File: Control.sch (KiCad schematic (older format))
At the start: 21 parts

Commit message: version preliminar de la etapa de alimentacion
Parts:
- gave numbers to parts that had none: 21
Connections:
- wire segments 81 -> 71

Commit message: asignacion inicial de huellas
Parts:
- added C37: 10n, Capacitors_SMD:C_0805, symbol C
- added C38, C39: 0,047n, Capacitors_SMD:C_0805, symbol C
- added D3: D_Schottky_ALT, Diodos:SOD-123, symbol D_Schottky_ALT
- added F2: F, Resistencias:R_1812, symbol F
- added L3: Ferrita, Capacitors_SMD:C_0805, symbol Ferrita
- added P15: USB_MINI, Conectores:usb_mini_molex_675031020, symbol USB_MINI
- added R60, R61: 22R, Resistencias:R_0805, symbol R
- C10, C5, C6, C8, C9: footprint (none) -> Capacitors_SMD:C_0805
- C11: footprint (none) -> Capacitors_SMD:C_1210
- C7: footprint (none) -> Capacitors_SMD:C_1206
- R10, R11, R3, R4, R5, R6, R7, R8, R9: footprint (none) -> Resistencias:R_0805
- U3: footprint (none) -> Housings_SSOP:SSOP-20_4.4x6.5mm_Pitch0.65mm
- U4: footprint (none) -> esp:ESP-12E
- Y1: footprint (none) -> Cristal:Cristal_SMD_HC49-SD; Fabricante (none) -> Fox Electronics; Provedor (none) -> rs; Ref (none) -> FOXSDLF/120-20; Ref_Proveedor (none) -> 547-6480
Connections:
- net labels added: VUSB
- wire segments 71 -> 90
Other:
- moved on the sheet: C10, C11, R3, R4, R5, R6, R7, U4

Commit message: cambiar ch340T por ch340g y añadir nc a pines
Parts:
- removed U3: CH340T, Housings_SSOP:SSOP-20_4.4x6.5mm_Pitch0.65mm, symbol CH340T
- added U3: CH340G, Housings_SOIC:SOIC-16_3.9x9.9mm_Pitch1.27mm, symbol CH340G
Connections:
- no-connect marks 7 -> 15
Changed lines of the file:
@@
 $Descr A4 11693 8268
 encoding utf-8
-Sheet 3 15
+Sheet 3 14
 Title ""
 Date "2017-01-15"
@@
 Comment4 "Wifi Play Board"
 $EndDescr
-$Comp
-L CH340T U3
-U 1 1 583CB227
-P 2550 3650
-F 0 "U3" H 2600 3600 60  0000 C CNN
-F 1 "CH340T" H 3000 4000 80  0000 C CNN
-F 2 "Housings_SSOP:SSOP-20_4.4x6.5mm_Pitch0.65mm" H 2750 3650 60  0001 C CNN
-F 3 "" H 2750 3650 60  0001 C CNN
-F 4 "~" H 2550 3650 60  0001 C CNN "Fabricante"
-F 5 "~" H 2550 3650 60  0001 C CNN "Ref"
-F 6 "~" H 2550 3650 60  0001 C CNN "Potencia"
-F 7 "~" H 2550 3650 60  0001 C CNN "Tolerancia"
-F 8 "~" H 2550 3650 60  0001 C CNN "Provedor"
-F 9 "~" H 2550 3650 60  0001 C CNN "Ref_Proveedor"
-	1    2550 3650
-	1    0    0    -1
-$EndComp
 $Comp
 L ESP8266 U4
@@
 Connection ~ 1350 3450
 $Comp
-L GND #PWR016
+L GND #PWR024
 U 1 1 583CD0A6
 P 1350 4050
-F 0 "#PWR016" H 1350 3800 50  0001 C CNN
+F 0 "#PWR024" H 1350 3800 50  0001 C CNN
 F 1 "GND" H 1355 3877 50  0000 C CNN
 F 2 "" H 1350 4050 50  0000 C CNN
@@
 $EndComp
 $Comp
-L GND #PWR017
+L GND #PWR025
 U 1 1 583CD111
 P 1950 4050
-F 0 "#PWR017" H 1950 3800 50  0001 C CNN
+F 0 "#PWR025" H 1950 3800 50  0001 C CNN
 F 1 "GND" H 1955 3877 50  0000 C CNN
 F 2 "" H 1950 4050 50  0000 C CNN
@@
 $EndComp
 $Comp
-L GND #PWR018
+L GND #PWR026
 U 1 1 583E093D
 P 9550 5300
-F 0 "#PWR018" H 9550 5050 50  0001 C CNN
+F 0 "#PWR026" H 9550 5050 50  0001 C CNN
 F 1 "GND" H 9555 5127 50  0000 C CNN
 F 2 "" H 9550 5300 50  0000 C CNN
@@
 	9550 5100 9450 5100
 $Comp
-L GND #PWR019
+L GND #PWR027
 U 1 1 583E0A57
 P 7400 5850
-F 0 "#PWR019" H 7400 5600 50  0001 C CNN
+F 0 "#PWR027" H 7400 5600 50  0001 C CNN
 F 1 "GND" H 7405 5677 50  0000 C CNN
 F 2 "" H 7400 5850 50  0000 C CNN
@@
 	7250 5100 7550 5100
 $Comp
-L +3V3 #PWR020
+L +3V3 #PWR028
 U 1 1 583F255D
 P 7250 5100
-F 0 "#PWR020" H 7250 4950 50  0001 C CNN
+F 0 "#PWR028" H 7250 4950 50  0001 C CNN
 F 1 "+3V3" V 7265 5228 50  0000 L CNN
 F 2 "" H 7250 5100 50  0000 C CNN
@@
 Connection ~ 7400 5100
 $Comp
-L +5V #PWR021
+L +5V #PWR029
 U 1 1 583F2750
 P 2900 1150
-F 0 "#PWR021" H 2900 1000 50  0001 C CNN
+F 0 "#PWR029" H 2900 1000 50  0001 C CNN
 F 1 "+5V" H 2915 1323 50  0000 C CNN
 F 2 "" H 2900 1150 50  0000 C CNN
@@
 Connection ~ 2900 1300
 $Comp
-L GND #PWR022
+L GND #PWR030
 U 1 1 583F287E
 P 2150 1800
-F 0 "#PWR022" H 2150 1550 50  0001 C CNN
+F 0 "#PWR030" H 2150 1550 50  0001 C CNN
 F 1 "GND" H 2155 1627 50  0000 C CNN
 F 2 "" H 2150 1800 50  0000 C CNN
@@
 	2550 1700 2550 1800
 $Comp
-L GND #PWR023
+L GND #PWR031
 U 1 1 583F2984
 P 2550 1800
-F 0 "#PWR023" H 2550 1550 50  0001 C CNN
+F 0 "#PWR031" H 2550 1550 50  0001 C CNN
 F 1 "GND" H 2555 1627 50  0000 C CNN
 F 2 "" H 2550 1800 50  0000 C CNN
@@
 $EndComp
 $Comp
-L GND #PWR024
+L GND #PWR032
 U 1 1 583F2B88
 P 3050 4000
-F 0 "#PWR024" H 3050 3750 50  0001 C CNN
+F 0 "#PWR032" H 3050 3750 50  0001 C CNN
 F 1 "GND" H 3055 3827 50  0000 C CNN
 F 2 "" H 3050 4000 50  0000 C CNN
@@
 $EndBitmap
 $Comp
-L +3V3 #PWR025
+L +3V3 #PWR033
 U 1 1 583F38C9
 P 7750 1100
-F 0 "#PWR025" H 7750 950 50  0001 C CNN
+F 0 "#PWR033" H 7750 950 50  0001 C CNN
 F 1 "+3V3" H 7765 1273 50  0000 C CNN
 F 2 "" H 7750 1100 50  0000 C CNN
@@
 	7750 2050 7750 2450
 $Comp
-L GND #PWR026
+L GND #PWR034
 U 1 1 583F42FE
 P 7750 2450
-F 0 "#PWR026" H 7750 2200 50  0001 C CNN
+F 0 "#PWR034" H 7750 2200 50  0001 C CNN
 F 1 "GND" H 7755 2277 50  0000 C CNN
 F 2 "" H 7750 2450 50  0000 C CNN
@@
 NoConn ~ 3750 2850
 NoConn ~ 2350 2850
-NoConn ~ 2350 2700
 Text Label 8700 1450 2    60   ~ 0
 GPIO2
@@
 Wire Wire Line
 	4150 2250 3750 2250
-NoConn ~ 3750 3450
-$Comp
-L GND #PWR027
+$Comp
+L GND #PWR035
 U 1 1 587ABB0C
 P 3550 1800
-F 0 "#PWR027" H 3550 1550 50  0001 C CNN
+F 0 "#PWR035" H 3550 1550 50  0001 C CNN
 F 1 "GND" H 3555 1627 50  0000 C CNN
 F 2 "" H 3550 1800 50  0000 C CNN
@@
 MOSI
 $Comp
-L GND #PWR028
+L GND #PWR036
 U 1 1 587BEF34
 P 9100 2450
-F 0 "#PWR028" H 9100 2200 50  0001 C CNN
+F 0 "#PWR036" H 9100 2200 50  0001 C CNN
 F 1 "GND" H 9105 2277 50  0000 C CNN
 F 2 "" H 9100 2450 50  0000 C CNN
@@
 	3200 7000 3200 6650
 $Comp
-L GND #PWR029
+L GND #PWR037
 U 1 1 5891BD78
 P 2150 7000
-F 0 "#PWR029" H 2150 6750 50  0001 C CNN
+F 0 "#PWR037" H 2150 6750 50  0001 C CNN
 F 1 "GND" H 2155 6827 50  0000 C CNN
 F 2 "" H 2150 7000 50  0000 C CNN
@@
 $EndComp
 $Comp
-L GND #PWR030
+L GND #PWR038
 U 1 1 5891BD7E
 P 2700 7000
-F 0 "#PWR030" H 2700 6750 50  0001 C CNN
+F 0 "#PWR038" H 2700 6750 50  0001 C CNN
 F 1 "GND" H 2705 6827 50  0000 C CNN
 F 2 "" H 2700 7000 50  0000 C CNN
@@
 $EndComp
 $Comp
-L GND #PWR031
+L GND #PWR039
 U 1 1 5891BD84
 P 3200 7000
-F 0 "#PWR031" H 3200 6750 50  0001 C CNN
+F 0 "#PWR039" H 3200 6750 50  0001 C CNN
 F 1 "GND" H 3205 6827 50  0000 C CNN
 F 2 "" H 3200 7000 50  0000 C CNN
@@
 	4800 5800 4800 5600
 $Comp
-L +5V #PWR032
+L +5V #PWR040
 U 1 1 5891BD93
 P 4800 5600
-F 0 "#PWR032" H 4800 5450 50  0001 C CNN
+F 0 "#PWR040" H 4800 5450 50  0001 C CNN
 F 1 "+5V" H 4815 5773 50  0000 C CNN
 F 2 "" H 4800 5600 50  0000 C CNN
@@
 	3600 5250 3600 5800
 Connection ~ 3600 5800
+$Comp
+L CH340G U3
+U 1 1 58965F58
+P 2550 3650
+F 0 "U3" H 2600 3550 60  0000 C CNN
+F 1 "CH340G" H 3050 4000 80  0000 C CNN
+F 2 "Housings_SOIC:SOIC-16_3.9x9.9mm_Pitch1.27mm" H -350 750 60  0001 C CNN
+F 3 "" H -350 750 60  0001 C CNN
+	1    2550 3650
+	1    0    0    -1
+$EndComp
+NoConn ~ 8200 5500
+NoConn ~ 8300 5500
+NoConn ~ 8400 5500
+NoConn ~ 8500 5500
+NoConn ~ 8600 5500
+NoConn ~ 8700 5500
+NoConn ~ 7250 4700
+NoConn ~ 7250 4500
+NoConn ~ 2050 6100
+NoConn ~ 1650 6400
 $EndSCHEMATC

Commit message: cambiado cristal de cuarzo por resonador
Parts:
- removed C5, C6: 0,022n, Capacitors_SMD:C_0805, symbol C
- removed L3: Ferrita, Capacitors_SMD:C_0805, symbol Ferrita
- removed Y1: 12MHz, Cristal:Cristal_SMD_HC49-SD, symbol Cristal_2P
- added Y1: Cristal, Cristal:Murata_CSTCE_V_A, symbol Cristal
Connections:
- wire segments 90 -> 88
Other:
- moved on the sheet: C7, D3, F2

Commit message: place inicial sobre la pcb
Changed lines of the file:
@@
 USBD-
 $Comp
-L GND #PWR026
+L GND #PWR024
 U 1 1 583CD0A6
 P 1350 3400
-F 0 "#PWR026" H 1350 3150 50  0001 C CNN
+F 0 "#PWR024" H 1350 3150 50  0001 C CNN
 F 1 "GND" H 1355 3227 50  0000 C CNN
 F 2 "" H 1350 3400 50  0000 C CNN
@@
 $EndComp
 $Comp
-L GND #PWR028
+L GND #PWR025
 U 1 1 583E093D
 P 9550 5300
-F 0 "#PWR028" H 9550 5050 50  0001 C CNN
+F 0 "#PWR025" H 9550 5050 50  0001 C CNN
 F 1 "GND" H 9555 5127 50  0000 C CNN
 F 2 "" H 9550 5300 50  0000 C CNN
@@
 	9550 5100 9450 5100
 $Comp
-L GND #PWR029
+L GND #PWR026
 U 1 1 583E0A57
 P 7400 5850
-F 0 "#PWR029" H 7400 5600 50  0001 C CNN
+F 0 "#PWR026" H 7400 5600 50  0001 C CNN
 F 1 "GND" H 7405 5677 50  0000 C CNN
 F 2 "" H 7400 5850 50  0000 C CNN
@@
 	7250 5100 7550 5100
 $Comp
-L +3V3 #PWR030
+L +3V3 #PWR027
 U 1 1 583F255D
 P 7250 5100
-F 0 "#PWR030" H 7250 4950 50  0001 C CNN
+F 0 "#PWR027" H 7250 4950 50  0001 C CNN
 F 1 "+3V3" V 7265 5228 50  0000 L CNN
 F 2 "" H 7250 5100 50  0000 C CNN
@@
 Connection ~ 7400 5100
 $Comp
-L +5V #PWR031
+L +5V #PWR028
 U 1 1 583F2750
 P 2550 1150
-F 0 "#PWR031" H 2550 1000 50  0001 C CNN
+F 0 "#PWR028" H 2550 1000 50  0001 C CNN
 F 1 "+5V" H 2565 1323 50  0000 C CNN
 F 2 "" H 2550 1150 50  0000 C CNN
@@
 $EndComp
 $Comp
-L GND #PWR032
+L GND #PWR029
 U 1 1 583F287E
 P 4500 6550
-F 0 "#PWR032" H 4500 6300 50  0001 C CNN
+F 0 "#PWR029" H 4500 6300 50  0001 C CNN
 F 1 "GND" H 4505 6377 50  0000 C CNN
 F 2 "" H 4500 6550 50  0000 C CNN
@@
 	2550 1700 2550 1800
 $Comp
-L GND #PWR033
+L GND #PWR030
 U 1 1 583F2984
 P 2550 1800
-F 0 "#PWR033" H 2550 1550 50  0001 C CNN
+F 0 "#PWR030" H 2550 1550 50  0001 C CNN
 F 1 "GND" H 2555 1627 50  0000 C CNN
 F 2 "" H 2550 1800 50  0000 C CNN
@@
 $EndComp
 $Comp
-L GND #PWR034
+L GND #PWR031
 U 1 1 583F2B88
 P 3050 4000
-F 0 "#PWR034" H 3050 3750 50  0001 C CNN
+F 0 "#PWR031" H 3050 3750 50  0001 C CNN
 F 1 "GND" H 3055 3827 50  0000 C CNN
 F 2 "" H 3050 4000 50  0000 C CNN
@@
 $EndBitmap
 $Comp
-L +3V3 #PWR035
+L +3V3 #PWR032
 U 1 1 583F38C9
 P 7750 1100
-F 0 "#PWR035" H 7750 950 50  0001 C CNN
+F 0 "#PWR032" H 7750 950 50  0001 C CNN
 F 1 "+3V3" H 7765 1273 50  0000 C CNN
 F 2 "" H 7750 1100 50  0000 C CNN
@@
 	7750 2050 7750 2450
 $Comp
-L GND #PWR036
+L GND #PWR033
 U 1 1 583F42FE
 P 7750 2450
-F 0 "#PWR036" H 7750 2200 50  0001 C CNN
+F 0 "#PWR033" H 7750 2200 50  0001 C CNN
 F 1 "GND" H 7755 2277 50  0000 C CNN
 F 2 "" H 7750 2450 50  0000 C CNN
@@
 	4150 2250 3750 2250
 $Comp
-L GND #PWR037
+L GND #PWR034
 U 1 1 587ABB0C
 P 3550 1800
-F 0 "#PWR037" H 3550 1550 50  0001 C CNN
+F 0 "#PWR034" H 3550 1550 50  0001 C CNN
 F 1 "GND" H 3555 1627 50  0000 C CNN
 F 2 "" H 3550 1800 50  0000 C CNN
@@
 MOSI
 $Comp
-L GND #PWR038
+L GND #PWR035
 U 1 1 587BEF34
 P 9100 2450
-F 0 "#PWR038" H 9100 2200 50  0001 C CNN
+F 0 "#PWR035" H 9100 2200 50  0001 C CNN
 F 1 "GND" H 9105 2277 50  0000 C CNN
 F 2 "" H 9100 2450 50  0000 C CNN
@@
 	3200 7000 3200 6650
 $Comp
-L GND #PWR039
+L GND #PWR036
 U 1 1 5891BD78
 P 2150 7000
-F 0 "#PWR039" H 2150 6750 50  0001 C CNN
+F 0 "#PWR036" H 2150 6750 50  0001 C CNN
 F 1 "GND" H 2155 6827 50  0000 C CNN
 F 2 "" H 2150 7000 50  0000 C CNN
@@
 $EndComp
 $Comp
-L GND #PWR040
+L GND #PWR037
 U 1 1 5891BD7E
 P 2700 7000
-F 0 "#PWR040" H 2700 6750 50  0001 C CNN
+F 0 "#PWR037" H 2700 6750 50  0001 C CNN
 F 1 "GND" H 2705 6827 50  0000 C CNN
 F 2 "" H 2700 7000 50  0000 C CNN
@@
 $EndComp
 $Comp
-L GND #PWR041
+L GND #PWR038
 U 1 1 5891BD84
 P 3200 7000
-F 0 "#PWR041" H 3200 6750 50  0001 C CNN
+F 0 "#PWR038" H 3200 6750 50  0001 C CNN
 F 1 "GND" H 3205 6827 50  0000 C CNN
 F 2 "" H 3200 7000 50  0000 C CNN
@@
 	5100 5800 5100 5600
 $Comp
-L +5V #PWR042
+L +5V #PWR039
 U 1 1 5891BD93
 P 5100 5600
-F 0 "#PWR042" H 5100 5450 50  0001 C CNN
+F 0 "#PWR039" H 5100 5450 50  0001 C CNN
 F 1 "+5V" H 5115 5773 50  0000 C CNN
 F 2 "" H 5100 5600 50  0000 C CNN
@@
 Connection ~ 2550 1300
 $Comp
-L +3V3 #PWR043
+L +3V3 #PWR040
 U 1 1 5896739C
 P 3550 1150
-F 0 "#PWR043" H 350 -100 50  0001 C CNN
+F 0 "#PWR040" H 350 -100 50  0001 C CNN
 F 1 "+3V3" H 3565 1323 50  0000 C CNN
 F 2 "" H 350 50  50  0001 C CNN
@@
 F 0 "Y1" V 1709 3381 50  0000 L CNN
 F 1 "Cristal" V 1800 3381 50  0000 L CNN
-F 2 "Cristal:Murata_CSTCE_V_A" V 1891 3381 50  0000 L CNN
+F 2 "Cristal:Murata_CSTCE_V_A" V 1891 3381 50  0001 L CNN
 F 3 "" H 1680 -640 50  0000 C CNN
 F 4 "murata" H 1800 3300 60  0001 C CNN "Fabricante"

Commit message: añadida LDR. Finalizado trazado provisional
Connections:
- net GND: now also P15.6 (shield)
- no-connect marks 15 -> 14
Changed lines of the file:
@@
 $Descr A4 11693 8268
 encoding utf-8
-Sheet 3 14
+Sheet 3 15
 Title ""
 Date "2017-01-15"
@@
 NoConn ~ 7250 4500
 NoConn ~ 2050 6100
-NoConn ~ 1650 6400
 Connection ~ 4500 5800
 Connection ~ 2550 1300
@@
 Wire Wire Line
 	1350 3300 1500 3300
+$Comp
+L GND #PWR?
+U 1 1 58A0B452
+P 1650 6550
+F 0 "#PWR?" H 1650 6300 50  0001 C CNN
+F 1 "GND" H 1655 6377 50  0000 C CNN
+F 2 "" H 1650 6550 50  0000 C CNN
+F 3 "" H 1650 6550 50  0000 C CNN
+	1    1650 6550
+	1    0    0    -1
+$EndComp
+Wire Wire Line
+	1650 6550 1650 6400
 $EndSCHEMATC

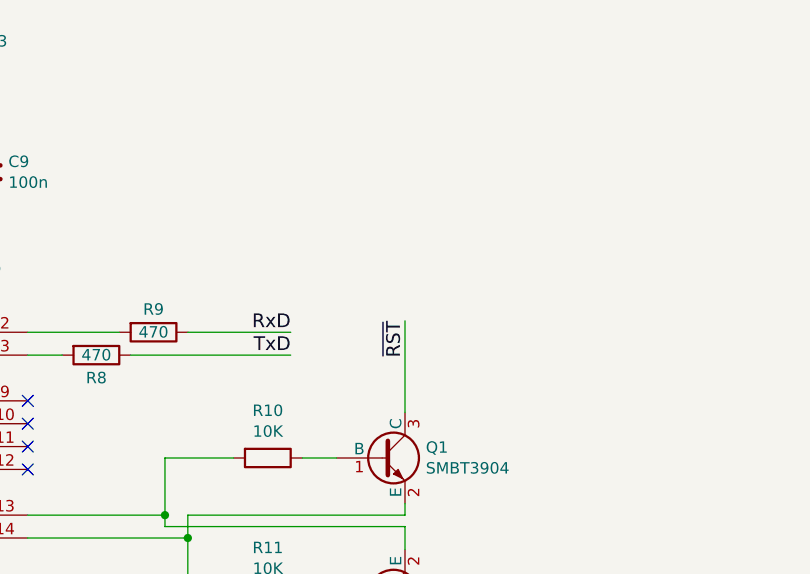
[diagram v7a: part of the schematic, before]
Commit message: conectar reset gpio. retocar plano masa
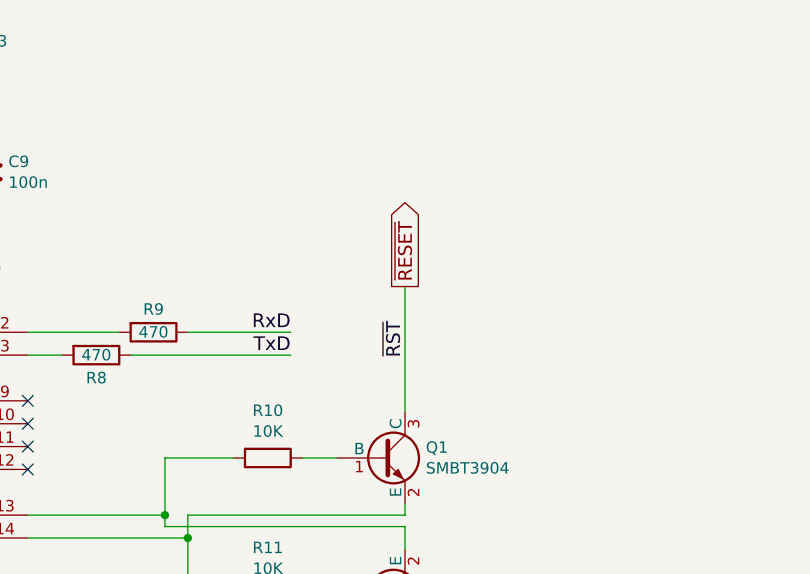
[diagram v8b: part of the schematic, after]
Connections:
- net ~RST renamed ~RESET
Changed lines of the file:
@@
 $Bitmap
 Pos 10950 6850
-Scale 0,350000
+Scale 0,000000
 Data
 89 50 4E 47 0D 0A 1A 0A 00 00 00 0D 49 48 44 52 00 00 01 D5 00 00 01 ED 08 06 00 00 00 4F 90 E4
@@
 	4350 2800 4650 2800
 Wire Wire Line
-	5400 2600 5400 2200
+	5400 2050 5400 2600
 Wire Wire Line
 	5400 3600 5400 4000
@@
 	1350 3300 1500 3300
 $Comp
-L GND #PWR?
+L GND #PWR040
 U 1 1 58A0B452
 P 1650 6550
-F 0 "#PWR?" H 1650 6300 50  0001 C CNN
+F 0 "#PWR040" H 1650 6300 50  0001 C CNN
 F 1 "GND" H 1655 6377 50  0000 C CNN
 F 2 "" H 1650 6550 50  0000 C CNN
@@
 Wire Wire Line
 	1650 6550 1650 6400
+Text GLabel 5400 2050 1    60   Output ~ 0
+~RESET
 $EndSCHEMATC
